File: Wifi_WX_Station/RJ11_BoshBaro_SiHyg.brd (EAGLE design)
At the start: 25.4 x 25.3 mm, 11 parts, among them U1 AS5030

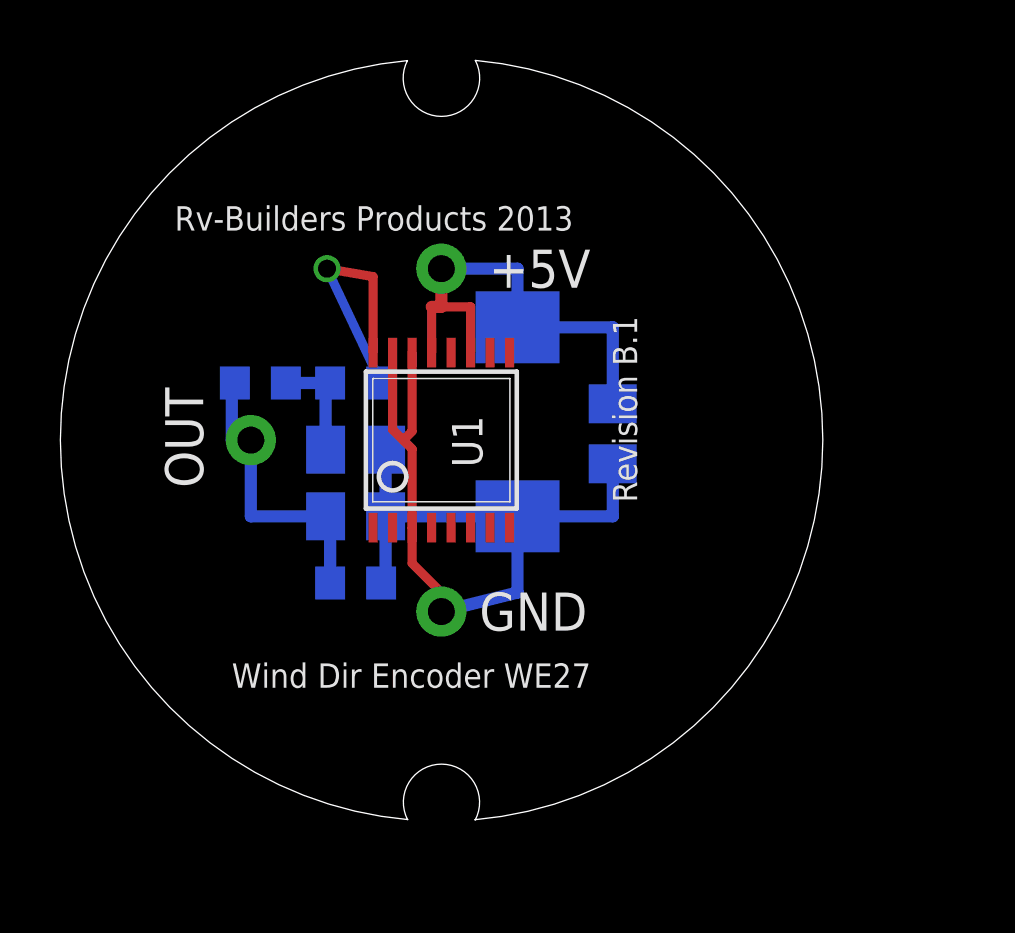
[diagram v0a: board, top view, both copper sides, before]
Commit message: added SILabs Hygrometer board Added frames to the schematics
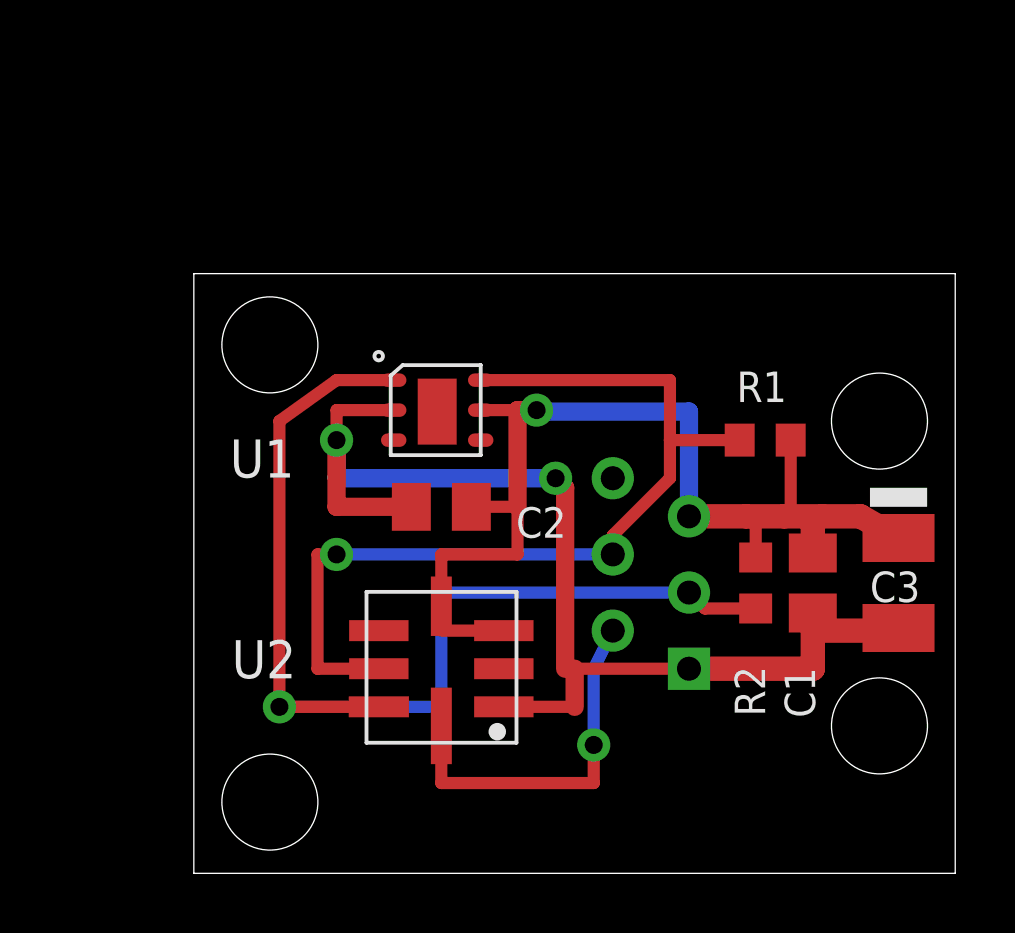
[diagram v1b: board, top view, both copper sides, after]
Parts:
- removed +5V, GND, OUT: TPSOL, wifi_WX:TP_SOL
- removed C5: 1uF, rcl:C0805K
- removed C6: 220uF/6.3V, rcl:SMC_D
- removed R6: 8.2K, rcl:R0603
- added C3: 22uF/10V, rcl:SMC_B
- added JP2: RJ11-6HOR_LP, wifi_WX:RJ11_HOR_LP
- added U2: (no value), 1AA_Stofer:LCC8
- C1, C2: value 1uF -> 100nF
- R1: value 6.8K -> 470o
- R2: value 26.1k -> 470o
- U1: value AS5030 -> SI7021-DFN6; device Stofer:TSSOP16 -> wifi_WX:DFN-6_SILABS
- moved R1 16.9 mm to (24.8, 14.0), flipped to the top, turned to 0 degrees
- moved R2 13.3 mm to (24.4, 9.21), flipped to the top, turned to 90 degrees
- moved C1 8.32 mm to (26.4, 9.21), flipped to the top
- moved C2 3.43 mm to (14.0, 11.7), flipped to the top
- moved U1 1.59 mm to (12.4, 14.0)
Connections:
- removed net N$1: +5V.P$1, C1.1, C6.+, U1.11, U1.13
- removed net N$2: C1.2, C2.2, C5.2, C6.-, GND.P$1, R2.2, U1.14, U1.15, U1.3
- removed net N$22: C2.1, R1.2, R6.1
- removed net N$23: R6.2, U1.16
- removed net N$3: C5.1, OUT.P$1, R1.1, R2.1
- new net +3V3: C1.1, C2.1, C3.+, JP2.P$5, R1.2, R2.2, U1.P$5, U2.P$3, U2.P$4
- new net GND: C1.2, C2.2, C3.-, JP2.P$1, U1.P$2, U2.P$1
- new net SCL: JP2.P$4, R1.1, U1.P$6, U2.P$6
- new net SDA: JP2.P$3, R2.1, U1.P$1, U2.P$7
- new net XCLR: JP2.P$2, U2.P$8
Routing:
- net GND: track 0.00 -> 39.3 mm, vias 0 -> 2
- net +3V3: track 0.00 -> 37.3 mm, vias 0 -> 1
- net SDA: track 0.00 -> 37.0 mm, vias 0 -> 1
- net N$2: track 31.3 -> 0.00 mm
- net SCL: track 0.00 -> 30.9 mm, vias 0 -> 1
- net N$1: track 15.8 -> 0.00 mm
- net XCLR: track 0.00 -> 12.2 mm, vias 0 -> 1
- net N$3: track 10.0 -> 0.00 mm
- net N$23: track 8.32 -> 0.00 mm, vias 1 -> 0
- net N$22: track 3.85 -> 0.00 mm
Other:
- board size 25.4 x 25.3 mm -> 25.4 x 20 mm
- board text added: "Baro-Temp-Hyg"
- board text added: "Rev B.2"
- board text added: "U2"
- board text added: "Wunder Weather 2014"
- board text removed: "+5V"
- board text removed: "GND"
- board text removed: "OUT"
- board text removed: "Revision B.1"
- board text removed: "Rv-Builders Products 2013"
- board text removed: "Wind Dir Encoder WE27"
